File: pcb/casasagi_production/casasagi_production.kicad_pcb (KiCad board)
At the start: 2 copper layers, 133.3 x 182.7 mm, 240 parts, among them J101 USB_C_Receptacle_USB2.0, J102 AudioJack4, J103 Conn_01x05, J201 USB_C_Receptacle_USB2.0, J202 AudioJack4, J203 Conn_01x05, SW101 RESET, SW102 BOOT, SW201 RESET, SW202 BOOT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

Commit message: Change boss thru hole to M2 thru hole
Introduce M2 thru hole to fix switch plate and PCB together using M2 screw. Spacer style boss can be placed at the edge cutout.
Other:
- outline, holes or cut-outs redrawn

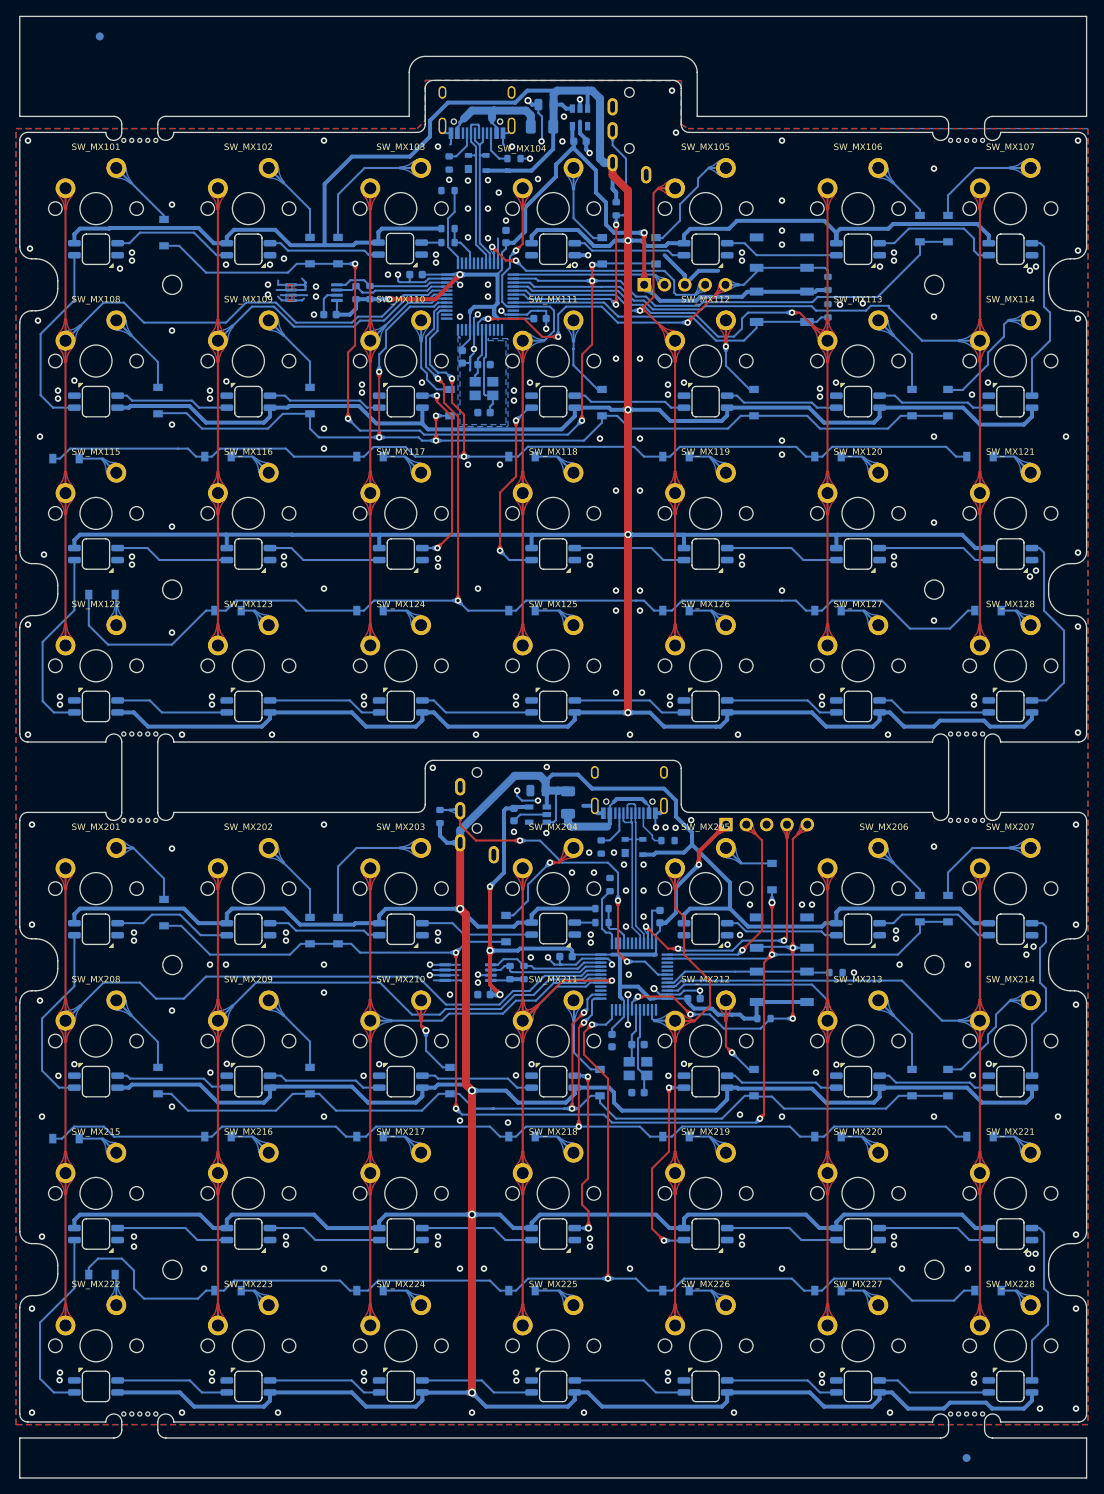
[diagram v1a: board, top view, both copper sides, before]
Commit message: replace M2 holes to drill holes
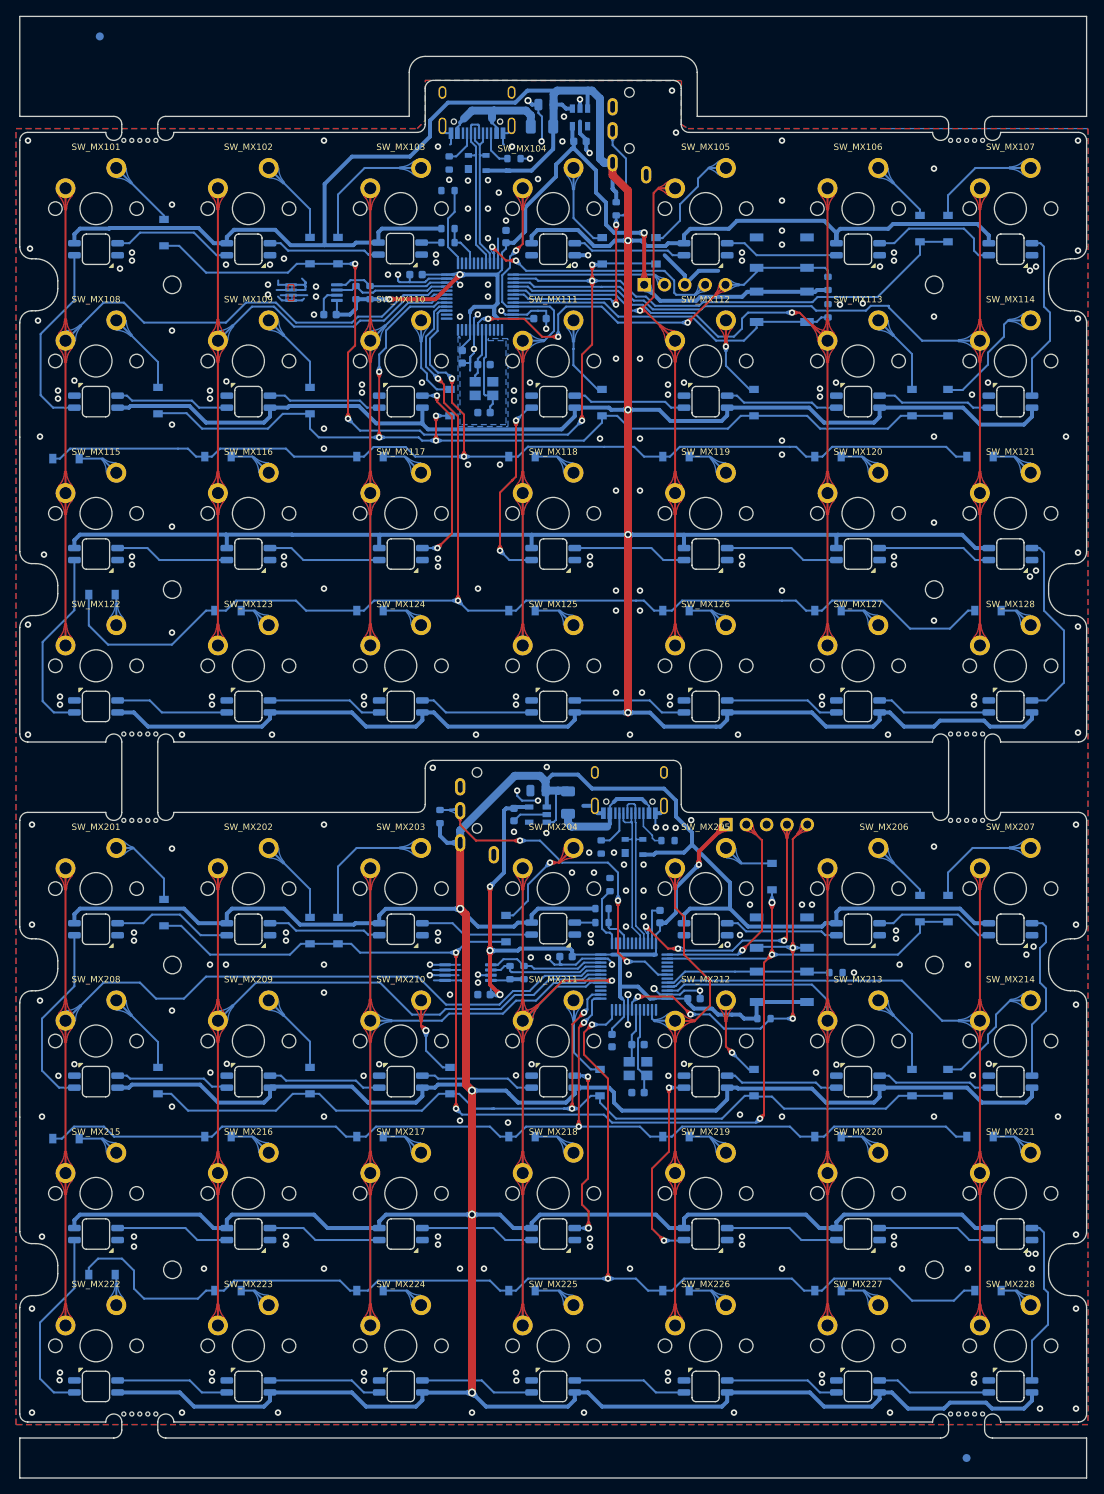
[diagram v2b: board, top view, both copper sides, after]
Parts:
- added REF**: MountingHole_2.2mm_M2, MountingHole:MountingHole_2.2mm_M2, F.Cu at (154.8, 182.7)
- added REF**: MountingHole_2.2mm_M2, MountingHole:MountingHole_2.2mm_M2, F.Cu at (59.5, 182.7)
- added REF**: MountingHole_2.2mm_M2, MountingHole:MountingHole_2.2mm_M2, F.Cu at (154.8, 144.6)
- added REF**: MountingHole_2.2mm_M2, MountingHole:MountingHole_2.2mm_M2, F.Cu at (59.5, 144.6)
- added REF**: MountingHole_2.2mm_M2, MountingHole:MountingHole_2.2mm_M2, F.Cu at (154.8, 97.6)
- added REF**: MountingHole_2.2mm_M2, MountingHole:MountingHole_2.2mm_M2, F.Cu at (59.5, 97.6)
- added REF**: MountingHole_2.2mm_M2, MountingHole:MountingHole_2.2mm_M2, F.Cu at (154.8, 59.5)
- added REF**: MountingHole_2.2mm_M2, MountingHole:MountingHole_2.2mm_M2, F.Cu at (59.5, 59.5)
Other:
- outline, holes or cut-outs redrawn
